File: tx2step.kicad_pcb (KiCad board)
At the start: 2 copper layers, 86.4 x 31.8 mm, 73 parts, among them CON1 BARREL_JACK, IC3 TPS61202, IC4 DRV8834, IC5 DRV8834, J1 Prog, J2 8P8C, J3 CHASSIS_SWITCHES, J4 6P4Cx2, SW1 SW_DIP_x02, SW2 SW_Push_Dual, U1 ATmega328P-MMH, U2 MCP73871-2AA, U3 ATtiny25V-10SSU, Y1 16 MHz

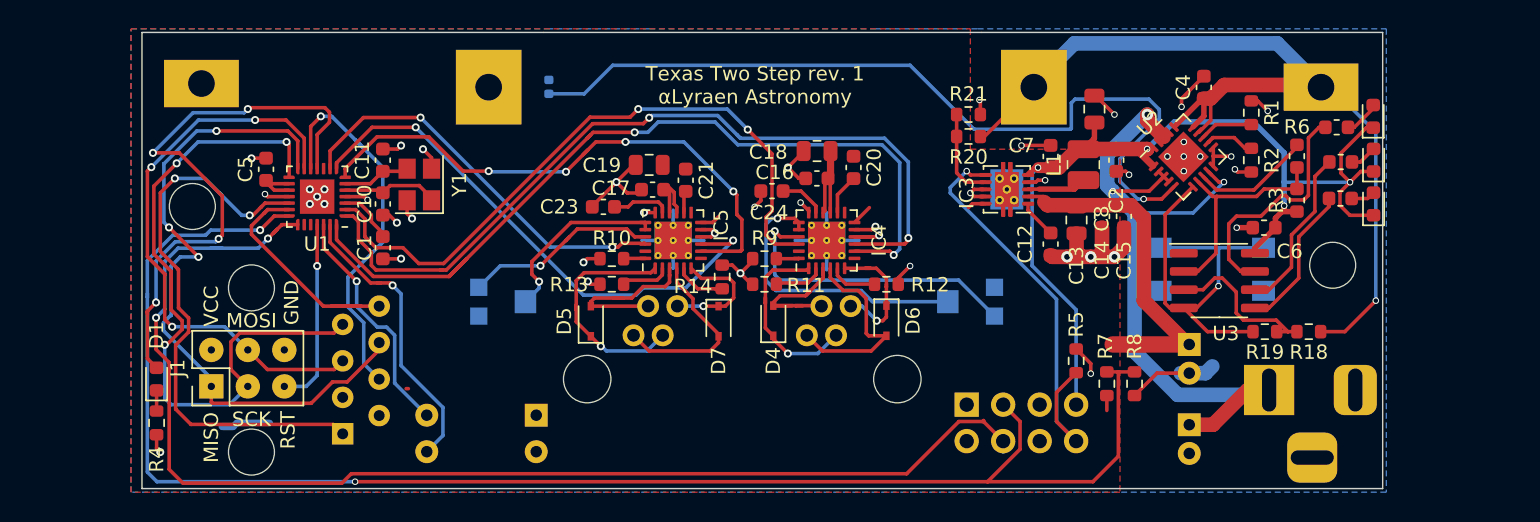
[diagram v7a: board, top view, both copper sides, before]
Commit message: Use FRE E5564 footprint for dual 6P4C
Less expensive part than the Molex, and leaves more room to lay out
the TVS diodes and ISEN resistors more nicely.
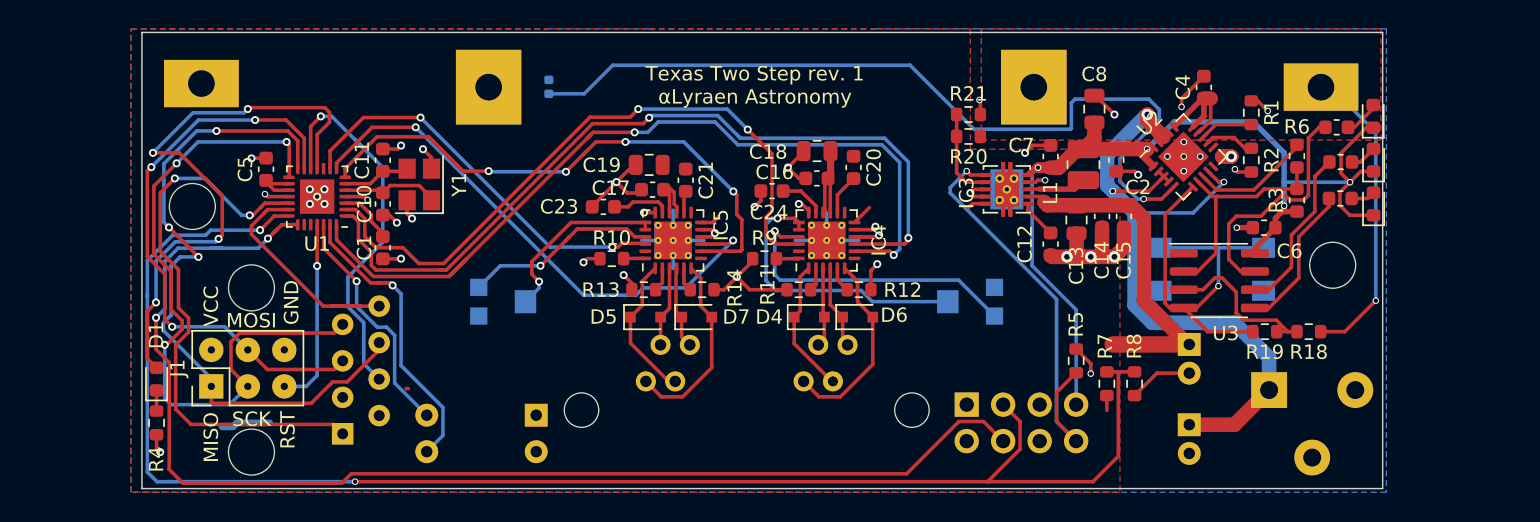
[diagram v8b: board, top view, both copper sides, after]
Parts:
- moved D5 3.82 mm to (143.5, 77.5), turned to 0 degrees
- moved D4 2.52 mm to (154.9, 77.5), turned to 0 degrees
- moved R11 2.42 mm to (154.2, 75.6)
- moved R13 2.25 mm to (143.4, 75.6)
- moved D6 2.01 mm to (158.3, 77.5), turned to 0 degrees
- moved R12 1.94 mm to (158.4, 75.6)
- moved R14 1.66 mm to (147.4, 75.6), turned to 180 degrees
- moved D7 1.55 mm to (147.1, 77.5), turned to 0 degrees
- moved J4 0.54 mm to (150.6, 83.9)
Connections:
- CON1 pad 3: GND -> (no net)
- IC4 pad 4: Net-(D6-Pad2) -> Net-(D6-Pad1)
- IC4 pad 6: Net-(D6-Pad1) -> Net-(D6-Pad2)
- IC5 pad 4: Net-(D7-Pad2) -> Net-(D7-Pad1)
- IC5 pad 6: Net-(D7-Pad1) -> Net-(D7-Pad2)
- J4 pad 1: Net-(D6-Pad1) -> Net-(D6-Pad2)
- J4 pad 2: Net-(D4-Pad1) -> Net-(D4-Pad2)
- J4 pad 3: Net-(D4-Pad2) -> Net-(D4-Pad1)
- J4 pad 4: Net-(D6-Pad2) -> Net-(D6-Pad1)
- J4 pad 5: Net-(D7-Pad1) -> Net-(D7-Pad2)
- J4 pad 6: Net-(D5-Pad1) -> Net-(D5-Pad2)
- J4 pad 7: Net-(D5-Pad2) -> Net-(D5-Pad1)
- J4 pad 8: Net-(D7-Pad2) -> Net-(D7-Pad1)
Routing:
- net +BATT: track 71.7 -> 36.3 mm
- net Net-(D5-Pad2): track 12.1 -> 5.59 mm
- net Net-(D5-Pad1): track 16.4 -> 10.1 mm, vias 1 -> 0
- net Net-(D4-Pad2): track 11.1 -> 5.55 mm
- net Net-(D4-Pad1): track 13.5 -> 9.45 mm, vias 1 -> 0
- net Net-(D6-Pad1): track 9.44 -> 5.83 mm, vias 1 -> 0
- net Net-(D7-Pad1): track 8.59 -> 5.78 mm, vias 1 -> 0
- net Net-(IC5-Pad5): track 3.53 -> 1.67 mm
- net Net-(IC5-Pad2): track 3.42 -> 1.69 mm
- net Net-(IC4-Pad2): track 3.36 -> 1.64 mm
- net GND: track 109.2 -> 107.4 mm
- net Net-(IC4-Pad5): track 3.43 -> 1.77 mm
- net +5V: track 48.9 -> 50.4 mm
- added copper zone on F.Cu, net +BATT
